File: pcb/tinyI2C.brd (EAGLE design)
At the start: 100 x 85 mm, 38 parts, among them IC1 74LVC1G125DCK, IC2 74LVC1G125DCK, IC3 IC_LDO_MIC5355, Q1 12MHz, U1 LPC824M201JHI33, X1 TSW-112-02-S-S, X2 TSW-112-02-S-S, X3 TSW-106-02-S-S-RA, X4 TSW-102-02-S-S, X5 TSW-102-02-S-S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

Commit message: update eagle version = 7.5.0; library update
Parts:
- TP3, TP7: value TPB1,27 -> TPTP14R; device testpad_local:B1,27 -> testpad_local:TP14R
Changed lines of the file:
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@@
 <?xml version="1.0" encoding="utf-8"?>
 <!DOCTYPE eagle SYSTEM "eagle.dtd">
-<eagle version="6.5.0">
+<eagle version="7.5.0">
 <drawing>
 <settings>
@@
 <layer number="29" name="tStop" color="7" fill="3" visible="yes" active="yes"/>
 <layer number="30" name="bStop" color="7" fill="6" visible="no" active="yes"/>
-<layer number="31" name="tCream" color="7" fill="4" visible="no" active="yes"/>
+<layer number="31" name="tCream" color="7" fill="4" visible="yes" active="yes"/>
 <layer number="32" name="bCream" color="7" fill="5" visible="no" active="yes"/>
 <layer number="33" name="tFinish" color="6" fill="3" visible="no" active="yes"/>
@@
 <layer number="101" name="PlacementGuide" color="7" fill="1" visible="no" active="yes"/>
 <layer number="102" name="Vscore" color="7" fill="1" visible="yes" active="yes"/>
-<layer number="103" name="not_populated" color="7" fill="1" visible="no" active="yes"/>
-<layer number="104" name="BottomSilkscreen" color="7" fill="1" visible="no" active="yes"/>
-<layer number="105" name="tPlate" color="7" fill="1" visible="no" active="yes"/>
-<layer number="106" name="bPlate" color="7" fill="1" visible="no" active="yes"/>
-<layer number="107" name="Crop" color="7" fill="1" visible="no" active="yes"/>
-<layer number="108" name="fp8" color="7" fill="1" visible="no" active="yes"/>
-<layer number="109" name="fp9" color="7" fill="1" visible="no" active="yes"/>
-<layer number="110" name="fp0" color="7" fill="1" visible="no" active="yes"/>
-<layer number="111" name="KASTMAAT1" color="7" fill="1" visible="no" active="yes"/>
-<layer number="112" name="KASTMAAT2" color="7" fill="1" visible="no" active="yes"/>
-<layer number="113" name="FRNTTEKEN" color="7" fill="1" visible="no" active="yes"/>
-<layer number="114" name="FRNTMAAT1" color="7" fill="1" visible="no" active="yes"/>
-<layer number="115" name="FRNTMAAT2" color="7" fill="1" visible="no" active="yes"/>
-<layer number="116" name="Patch_BOT" color="9" fill="4" visible="no" active="yes"/>
-<layer number="117" name="BACKMAAT1" color="7" fill="1" visible="no" active="yes"/>
-<layer number="118" name="BACKMAAT2" color="7" fill="1" visible="no" active="yes"/>
-<layer number="119" name="KAP_TEKEN" color="7" fill="1" visible="no" active="yes"/>
-<layer number="120" name="KAP_MAAT1" color="7" fill="1" visible="no" active="yes"/>
-<layer number="121" name="_tsilk" color="7" fill="1" visible="no" active="yes"/>
-<layer number="122" name="_bsilk" color="7" fill="1" visible="no" active="yes"/>
-<layer number="123" name="tTestmark" color="7" fill="1" visible="no" active="yes"/>
-<layer number="124" name="bTestmark" color="7" fill="1" visible="no" active="yes"/>
-<layer number="125" name="_tNames" color="7" fill="1" visible="no" active="yes"/>
-<layer number="126" name="BIFRNTMAT" color="7" fill="1" visible="no" active="yes"/>
-<layer number="127" name="_tValues" color="7" fill="1" visible="no" active="yes"/>
-<layer number="128" name="_bValues" color="7" fill="1" visible="no" active="yes"/>
-<layer number="130" name="SMDSTROOK" color="7" fill="1" visible="no" active="yes"/>
-<layer number="131" name="tAdjust" color="7" fill="1" visible="no" active="yes"/>
-<layer number="132" name="bAdjust" color="7" fill="1" visible="no" active="yes"/>
-<layer number="144" name="Drill_legend" color="7" fill="1" visible="no" active="yes"/>
-<layer number="145" name="DrillLegend_01-16" color="2" fill="9" visible="no" active="yes"/>
-<layer number="146" name="DrillLegend_01-20" color="3" fill="9" visible="no" active="yes"/>
-<layer number="151" name="HeatSink" color="7" fill="1" visible="no" active="yes"/>
-<layer number="152" name="_bDocu" color="7" fill="1" visible="no" active="yes"/>
-<layer number="199" name="Contour" color="7" fill="1" visible="no" active="yes"/>
-<layer number="200" name="200bmp" color="7" fill="1" visible="no" active="yes"/>
 <layer number="201" name="201bmp" color="2" fill="1" visible="no" active="no"/>
 <layer number="202" name="202bmp" color="3" fill="1" visible="no" active="no"/>
-<layer number="203" name="203bmp" color="4" fill="10" visible="no" active="yes"/>
-<layer number="204" name="204bmp" color="5" fill="10" visible="no" active="yes"/>
-<layer number="205" name="205bmp" color="6" fill="10" visible="no" active="yes"/>
-<layer number="206" name="206bmp" color="7" fill="10" visible="no" active="yes"/>
-<layer number="207" name="207bmp" color="8" fill="10" visible="no" active="yes"/>
-<layer number="208" name="208bmp" color="9" fill="10" visible="no" active="yes"/>
-<layer number="209" name="209bmp" color="7" fill="1" visible="no" active="yes"/>
-<layer number="210" name="210bmp" color="7" fill="1" visible="no" active="yes"/>
-<layer number="211" name="211bmp" color="7" fill="1" visible="no" active="yes"/>
-<layer number="212" name="212bmp" color="7" fill="1" visible="no" active="yes"/>
-<layer number="213" name="213bmp" color="7" fill="1" visible="no" active="yes"/>
-<layer number="214" name="214bmp" color="7" fill="1" visible="no" active="yes"/>
-<layer number="215" name="215bmp" color="7" fill="1" visible="no" active="yes"/>
-<layer number="216" name="216bmp" color="7" fill="1" visible="no" active="yes"/>
-<layer number="217" name="217bmp" color="7" fill="1" visible="no" active="yes"/>
-<layer number="218" name="218bmp" color="7" fill="1" visible="no" active="yes"/>
-<layer number="219" name="219bmp" color="7" fill="1" visible="no" active="yes"/>
-<layer number="220" name="220bmp" color="7" fill="1" visible="no" active="yes"/>
-<layer number="221" name="221bmp" color="7" fill="1" visible="no" active="yes"/>
-<layer number="222" name="imagesize" color="7" fill="1" visible="no" active="yes"/>
-<layer number="223" name="223bmp" color="7" fill="1" visible="no" active="yes"/>
-<layer number="224" name="224bmp" color="7" fill="1" visible="no" active="yes"/>
-<layer number="230" name="230bmp" color="7" fill="1" visible="no" active="yes"/>
-<layer number="248" name="Housing" color="7" fill="1" visible="no" active="yes"/>
-<layer number="249" name="Edge" color="7" fill="1" visible="no" active="yes"/>
-<layer number="250" name="Descript" color="7" fill="1" visible="no" active="yes"/>
-<layer number="251" name="SMDround" color="7" fill="1" visible="no" active="yes"/>
-<layer number="254" name="cooling" color="7" fill="1" visible="no" active="yes"/>
-<layer number="255" name="Accent" color="7" fill="1" visible="no" active="yes"/>
 </layers>
 <board>
@@
 <wire x1="26" y1="19.6" x2="26.7" y2="18.9" width="0.2" layer="21"/>
 <wire x1="26" y1="18.9" x2="26.7" y2="18.9" width="0.2" layer="21"/>
-<text x="19.8" y="13.8" size="1" layer="21" font="vector" ratio="20">GND</text>
+<text x="19.8" y="13.7" size="1" layer="21" font="vector" ratio="20">GND</text>
 <circle x="18.9" y="29.1" radius="0.3" width="0.2" layer="21"/>
 <circle x="22.4" y="20.9" radius="0.3" width="0.2" layer="21"/>
@@
 <dimension x1="5.6" y1="43" x2="5.6" y2="42" x3="-5" y3="42.5" textsize="1.778" layer="47" visible="yes"/>
 <dimension x1="5.6" y1="11" x2="5.6" y2="10" x3="-5" y3="10.5" textsize="1.778" layer="47" visible="yes"/>
+<rectangle x1="18.7" y1="28.9" x2="19.1" y2="29.3" layer="21"/>
+<rectangle x1="24.3" y1="20.7" x2="24.7" y2="21.1" layer="21"/>
+<rectangle x1="22.2" y1="20.7" x2="22.6" y2="21.1" layer="21"/>
 </plain>
 <attributes>
@@
 <param name="mvStopFrame" value="1"/>
 <param name="mvCreamFrame" value="0"/>
-<param name="mlMinStopFrame" value="4mil"/>
-<param name="mlMaxStopFrame" value="4mil"/>
+<param name="mlMinStopFrame" value="0.05mm"/>
+<param name="mlMaxStopFrame" value="0.05mm"/>
 <param name="mlMinCreamFrame" value="0mil"/>
 <param name="mlMaxCreamFrame" value="0mil"/>
@@
 <pass name="Default">
 <param name="RoutingGrid" value="50mil"/>
+<param name="AutoGrid" value="1"/>
+<param name="Efforts" value="0"/>
+<param name="TopRouterVariant" value="1"/>
 <param name="tpViaShape" value="round"/>
 <param name="PrefDir.1" value="|"/>
@@
 <attribute name="VALUE" x="15.046" y="35.892" size="0.0254" layer="27"/>
 </element>
-<element name="TP3" library="testpad_local" package="B1,27" value="TPB1,27" x="19.2" y="15.1" smashed="yes">
+<element name="TP3" library="testpad_local" package="TP14R" value="TPTP14R" x="19.2" y="15.1" smashed="yes">
 <attribute name="TP_SIGNAL_NAME" value="" x="19.2" y="13.195" size="1" layer="37"/>
 <attribute name="VALUE" x="18.946" y="14.592" size="0.0254" layer="27"/>
@@
 </element>
 <element name="C6" library="mylib" package="C0402" value="0.1u/1005" x="19.4" y="18.7" smashed="yes" rot="R270">
-<attribute name="NAME" x="20.7" y="15.5" size="1" layer="25" font="vector" ratio="20" rot="R90"/>
+<attribute name="NAME" x="20.7" y="15.6" size="1" layer="25" font="vector" ratio="20" rot="R90"/>
 <attribute name="VALUE" x="17.495" y="19.335" size="1.27" layer="27" rot="R270"/>
 </element>
@@
 <attribute name="VALUE" x="17.235" y="16.405" size="1.27" layer="27" rot="R180"/>
 </element>
-<element name="TP7" library="testpad_local" package="B1,27" value="TPB1,27" x="19.2" y="15.1" smashed="yes" rot="MR0">
+<element name="TP7" library="testpad_local" package="TP14R" value="TPTP14R" x="19.2" y="15.1" smashed="yes" rot="MR0">
 <attribute name="TP_SIGNAL_NAME" value="" x="19.835" y="13.195" size="1" layer="38" rot="MR0"/>
 <attribute name="VALUE" x="19.835" y="14.338" size="0.0254" layer="28" rot="MR0"/>
@@
 <via x="13.1" y="35.3" extent="1-16" drill="0.3"/>
 <via x="17.6" y="36.6" extent="1-16" drill="0.3"/>
-<via x="19.2" y="36.6" extent="1-16" drill="0.3"/>
+<via x="19.1" y="36.6" extent="1-16" drill="0.3"/>
 <polygon width="0.25" layer="1" thermals="no" rank="2">
 <vertex x="12.1" y="35.4"/>
@@
 <via x="19.2" y="15.1" extent="1-16" drill="0.8"/>
 <contactref element="TP7" pad="TP"/>
-<wire x1="19.2" y1="15.1" x2="19.2" y2="17.2" width="1.27" layer="1"/>
+<wire x1="19.2" y1="15.1" x2="19.2" y2="17.2" width="1.4" layer="1"/>
 <wire x1="19.2" y1="17.2" x2="19.4" y2="17.4" width="0.8" layer="1"/>
 <polygon width="0.25" layer="1" thermals="no" rank="2">

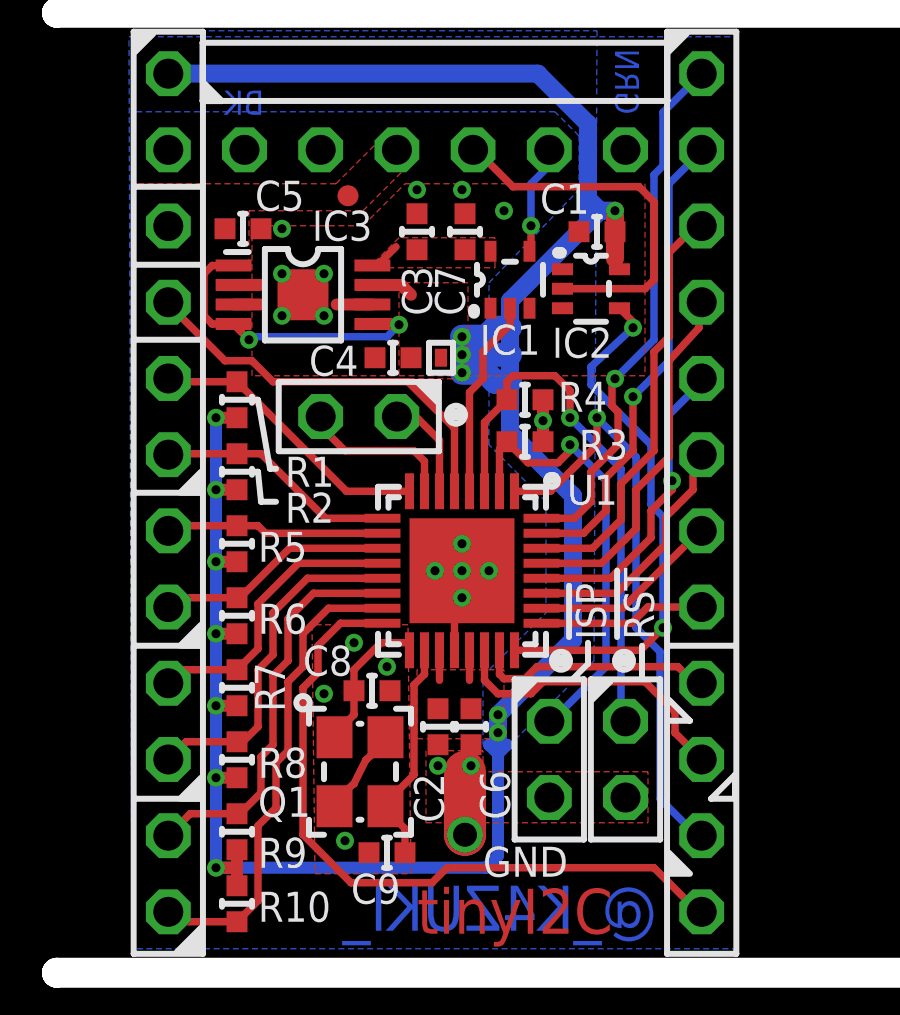
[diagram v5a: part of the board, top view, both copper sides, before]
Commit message: [ PCB ] library update
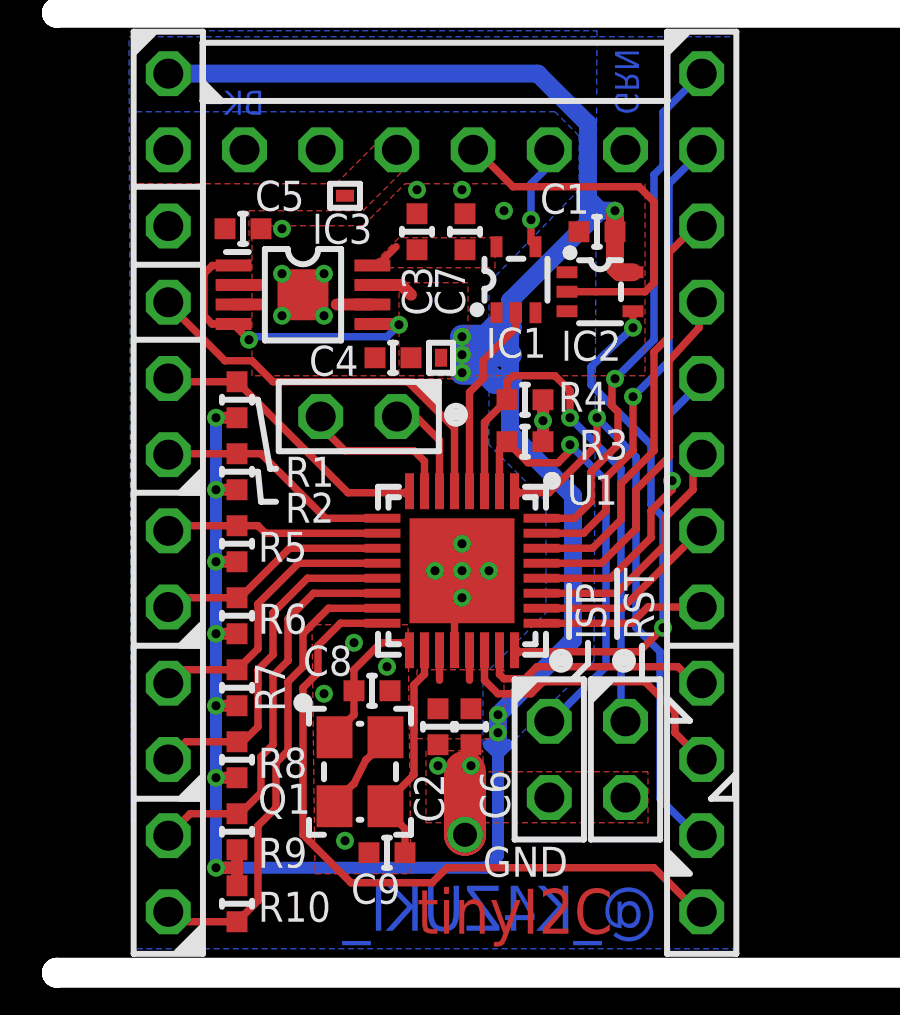
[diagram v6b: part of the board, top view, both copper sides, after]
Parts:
- removed TP1: TPTP07R, testpad_local:TP07R
- added TP6: TESTPAD, mylib:TP06RECT
- IC1, IC2: value 74LVC1G125DCK -> (none); device 74xx-little-us_local:SC70-5 -> mylib:IC_05_0.635_40MIL
- IC3: value IC_LDO_MIC5355 -> (none)
- Q1: value 12MHz -> (none); device adafruit (1):NX3225 -> mylib:CLOCK_3225
- moved IC2 0.32 mm to (23.7, 33.2)
- moved IC1 0.20 mm to (20.9, 33.6)
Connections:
- net 5V: now also TP6.TP; no longer TP1.TP
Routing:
- net 1.8V: track 88.6 -> 89.1 mm
